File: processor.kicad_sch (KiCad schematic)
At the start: 84 parts, among them J1 Cartrige, Q1 2N3904, Q2 2N3904, Q3 2N3904, Q4 2N3904, Q5 2N3904, SW1 RESET, U1 68000, U2 27C010, U3 27C010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

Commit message: motherboard: Added more footprints for parts and refined the serial comms section further
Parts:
- U2, U3: MFR (none) -> 3M; MPN (none) -> 4832-6000-CP; OC_FARNELL (none) -> 2672309
- U39: footprint Package_LCC:PLCC-68_SMD-Socket -> rhais_package-plcc:PLCC-68_SMD-Socket; MFR (none) -> Multicomp; MPN (none) -> MC-68PLCC-SMT; OC_FARNELL (none) -> 2097224
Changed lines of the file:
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@@
 			)
 		)
-		(property "MFR" ""
+		(property "MFR" "3M"
 			(at 241.3 203.2 0)
 			(effects
@@
 			)
 		)
-		(property "MPN" ""
+		(property "MPN" "4832-6000-CP"
 			(at 241.3 203.2 0)
 			(effects
@@
 			)
 		)
-		(property "OC_FARNELL" ""
+		(property "OC_FARNELL" "2672309"
 			(at 241.3 203.2 0)
 			(effects
@@
 			)
 		)
-		(property "Footprint" "Package_LCC:PLCC-68_SMD-Socket"
+		(property "Footprint" "rhais_package-plcc:PLCC-68_SMD-Socket"
 			(at 317.5 177.8 0)
 			(effects
@@
 			)
 		)
+		(property "MFR" "Multicomp"
+			(at 317.5 177.8 0)
+			(effects
+				(font
+					(size 1.27 1.27)
+				)
+				(hide yes)
+			)
+		)
+		(property "MPN" "MC-68PLCC-SMT"
+			(at 317.5 177.8 0)
+			(effects
+				(font
+					(size 1.27 1.27)
+				)
+				(hide yes)
+			)
+		)
+		(property "OC_FARNELL" "2097224"
+			(at 317.5 177.8 0)
+			(effects
+				(font
+					(size 1.27 1.27)
+				)
+				(hide yes)
+			)
+		)
 		(pin "56"
 		)
@@
 			)
 		)
-		(property "MFR" ""
+		(property "MFR" "3M"
 			(at 190.5 203.2 0)
 			(effects
@@
 			)
 		)
-		(property "MPN" ""
+		(property "MPN" "4832-6000-CP"
 			(at 190.5 203.2 0)
 			(effects
@@
 			)
 		)
-		(property "OC_FARNELL" ""
+		(property "OC_FARNELL" "2672309"
 			(at 190.5 203.2 0)
 			(effects

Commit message: motherboard: Sorted some of the clock generation circuitry out
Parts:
- removed unit 1 of U4
- removed unit 3 of U4
- Y1: value 4.433618MHz -> 4.433619MHz; footprint (none) -> Crystal:Crystal_SMD_HC49-SD; symbol Device:Crystal_GND23_Small -> Device:Crystal_Small; MFR (none) -> Ecliptek; MPN (none) -> E1SJA18-4.433619MTR; OC_FARNELL (none) -> 3264306
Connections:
- net GND: now also Y2.2; no longer Y1.2, Y1.3
- net at C12.1, Q1.B, R4.2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: now also Y1.2; no longer Y1.4
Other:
- moved on the sheet: C10, C11, C12, C13, C14, C15, C16, C17, C18, C19, C20, C21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

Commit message: motherboard: Sorted out all the 1N914's having found a suitable part
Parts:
- D1: footprint (none) -> Diode_SMD:D_SOD-323F; MFR (none) -> Onsemi; MPN (none) -> 1N914BWS; OC_FARNELL (none) -> 2453274
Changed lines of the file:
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@@
 			)
 		)
-		(property "Footprint" ""
+		(property "Footprint" "Diode_SMD:D_SOD-323F"
 			(at 68.58 53.34 90)
 			(effects
@@
 			)
 		)
-		(property "Datasheet" "~"
+		(property "Datasheet" "https://www.onsemi.com/download/data-sheet/pdf/1n4148ws-d.pdf"
 			(at 68.58 53.34 90)
 			(effects
@@
 			)
 		)
-		(property "MFR" ""
+		(property "MFR" "Onsemi"
 			(at 68.58 53.34 0)
 			(effects
@@
 			)
 		)
-		(property "MPN" ""
+		(property "MPN" "1N914BWS"
 			(at 68.58 53.34 0)
 			(effects
@@
 			)
 		)
-		(property "OC_FARNELL" ""
+		(property "OC_FARNELL" "2453274"
 			(at 68.58 53.34 0)
 			(effects

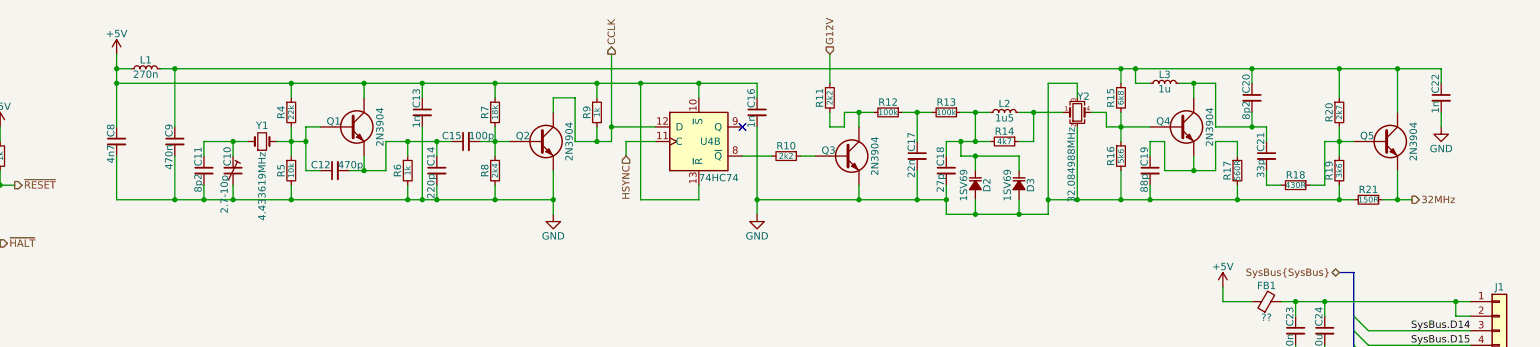
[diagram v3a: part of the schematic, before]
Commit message: motherboard: Cleaned up the clock tree implementation, specifying and fixing down how to do the 32MHz clock source
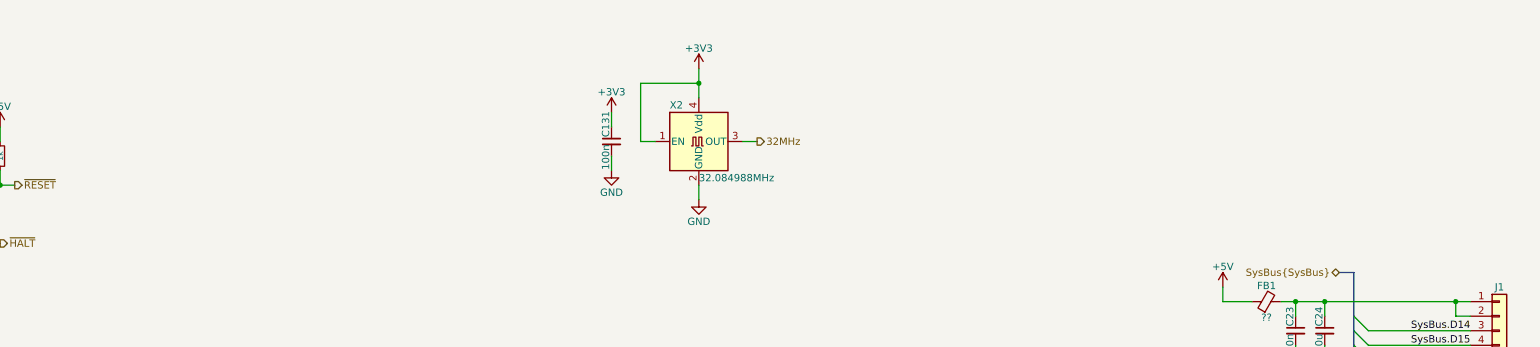
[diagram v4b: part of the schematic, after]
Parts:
- removed C10: 2.7-10p, symbol Device:C_Trim_Small
- removed C11, C20: 8p2, rhais_rcl:C0603, symbol Device:C_Small
- removed C12: 470p, rhais_rcl:C0603, symbol Device:C_Small
- removed C13, C16, C22: 1n, rhais_rcl:C0603, symbol Device:C_Small
- removed C14: 220p, rhais_rcl:C0603, symbol Device:C_Small
- removed C15: 100p, rhais_rcl:C0603, symbol Device:C_Small
- removed C17: 22n, rhais_rcl:C0603, symbol Device:C_Small
- removed C18: 27p, rhais_rcl:C0603, symbol Device:C_Small
- removed C19: 88p, rhais_rcl:C0603, symbol Device:C_Small
- removed C21: 33p, rhais_rcl:C0603, symbol Device:C_Small
- removed C8: 4n7, rhais_rcl:C0603, symbol Device:C_Small
- removed C9: 470n, rhais_rcl:C0603, symbol Device:C_Small
- removed D2, D3: 1SV69, symbol dragonmux:D_Cap_Small_Filled
- removed L1: 270n, symbol Device:L_Small
- removed L2: 1u5, symbol Device:L_Small
- removed L3: 1u, symbol Device:L_Small
- removed Q1, Q2, Q3, Q4, Q5: 2N3904, rhais_package-smd:SOT-23, symbol Device:Q_NPN
- removed R10, R11: 2k2, rhais_rcl:R0603, symbol Device:R_Small
- removed R12, R13: 100k, rhais_rcl:R0603, symbol Device:R_Small
- removed R14: 4k7, rhais_rcl:R0603, symbol Device:R_Small
- removed R15: 6k8, rhais_rcl:R0603, symbol Device:R_Small
- removed R16: 5k6, rhais_rcl:R0603, symbol Device:R_Small
- removed R17: 560R, rhais_rcl:R0603, symbol Device:R_Small
- removed R18: 430R, rhais_rcl:R0603, symbol Device:R_Small
- removed R19: 3k6, rhais_rcl:R0603, symbol Device:R_Small
- removed R20: 2k7, rhais_rcl:R0603, symbol Device:R_Small
- removed R21: 150R, rhais_rcl:R0603, symbol Device:R_Small
- removed R4: 22k, rhais_rcl:R0603, symbol Device:R_Small
- removed R5: 10k, rhais_rcl:R0603, symbol Device:R_Small
- removed R6, R9: 1k, rhais_rcl:R0603, symbol Device:R_Small
- removed R7: 18k, rhais_rcl:R0603, symbol Device:R_Small
- removed R8: 2k4, rhais_rcl:R0603, symbol Device:R_Small
- removed U4: 74HC74, rhais_package-smd:SO-14_3.9x8.65mm_P1.27mm, symbol 74xx:74LS74
- removed Y1: 4.433619MHz, Crystal:Crystal_SMD_HC49-SD, symbol Device:Crystal_Small
- removed Y2: 32.084988MHz, symbol Device:Crystal_GND23_Small
- added C131: 100n, rhais_rcl:C0603, symbol Device:C_Small
- added X2: 32.084988MHz, rhais_osc:SMD3225, symbol DX-MON:TXC-8W
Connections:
- net 32MHz: now also X2.3 (OUT)
- net GND: now also C131.2, X2.2 (GND)
- new net +3V3: C131.1, X2.1 (EN), X2.4 (Vdd)
- no-connect marks 2 -> 1
